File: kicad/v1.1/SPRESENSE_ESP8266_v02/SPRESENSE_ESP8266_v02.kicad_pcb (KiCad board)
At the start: 2 copper layers, 24.6 x 22.4 mm, 24 parts, among them J1 JP1, J2 JP2, Q1 BSS138, Q2 BSS138, SW1 RESET, SW2 PRG, U1 MIC5219-3.3BM5, U300 ESP-WROM-02

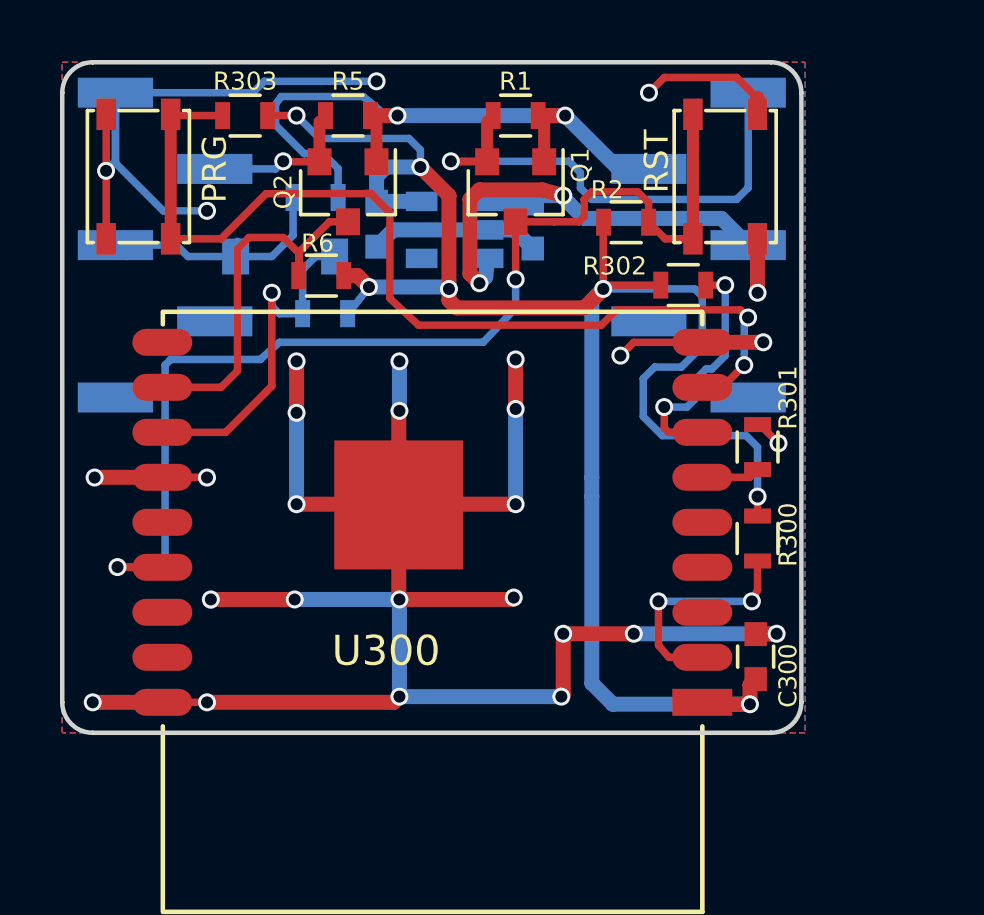
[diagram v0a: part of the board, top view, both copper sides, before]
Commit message: Refactor: Reorganize repository structure and add English README
- Add .gitignore to exclude macOS metadata and backup files
- Add README_EN.md with English translation and cross-link
- Move AT command PDFs to ESP8266_AT_command/ directory
- Reorganize examples under versioned directories (v1.1/, v2.2/)
- Add v2.2 examples with LINE messaging API and PIR sensor demo
- Move KiCad files to versioned directories and add v2.2 schematics
- Add product images to img/ directory
- Update README.md with detailed project overview and cross-link
- Remove macOS ._*/.DS_Store files and other temporary artifacts
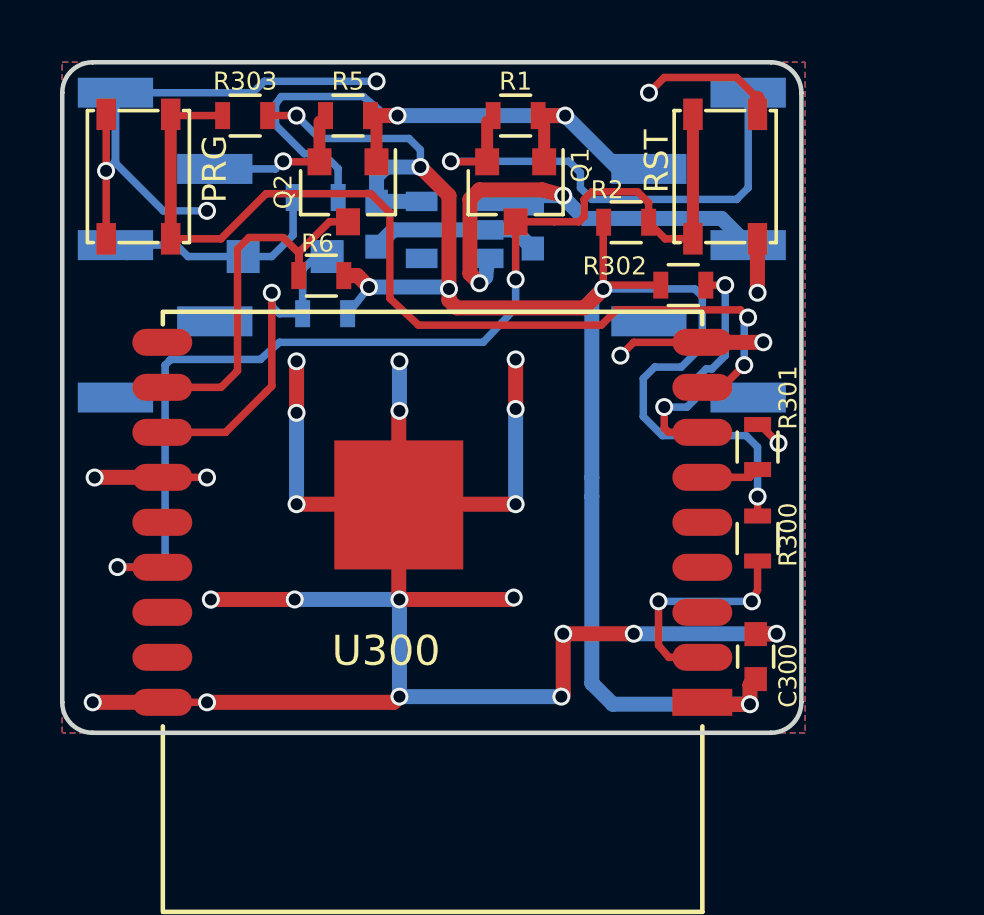
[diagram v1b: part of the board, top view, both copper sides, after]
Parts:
- removed G***: OSHW-logo_silkscreen-front_2mm, footprint:OSHW-logo_silkscreen-front_2mm
- D1: footprint Diodes_SMD:D_SOD-123 -> Diodes_SMD:D_SOD-123F
- moved ref** 2.67 mm to (141.4, 115.8)
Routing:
- net /UART2_RX: track 9.05 -> 8.49 mm
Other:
- net class Default removed
- board text added: "Wifi Shield v 1.1"
- board text removed: "SPRESENSE Wifi Shield v 1.1"
